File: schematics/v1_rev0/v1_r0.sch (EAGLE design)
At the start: 46 parts, among them Q1 LPM2302, Q2 LPM2302, Q3 16MHz, U1 ATMEGA*, U2 TMP36F

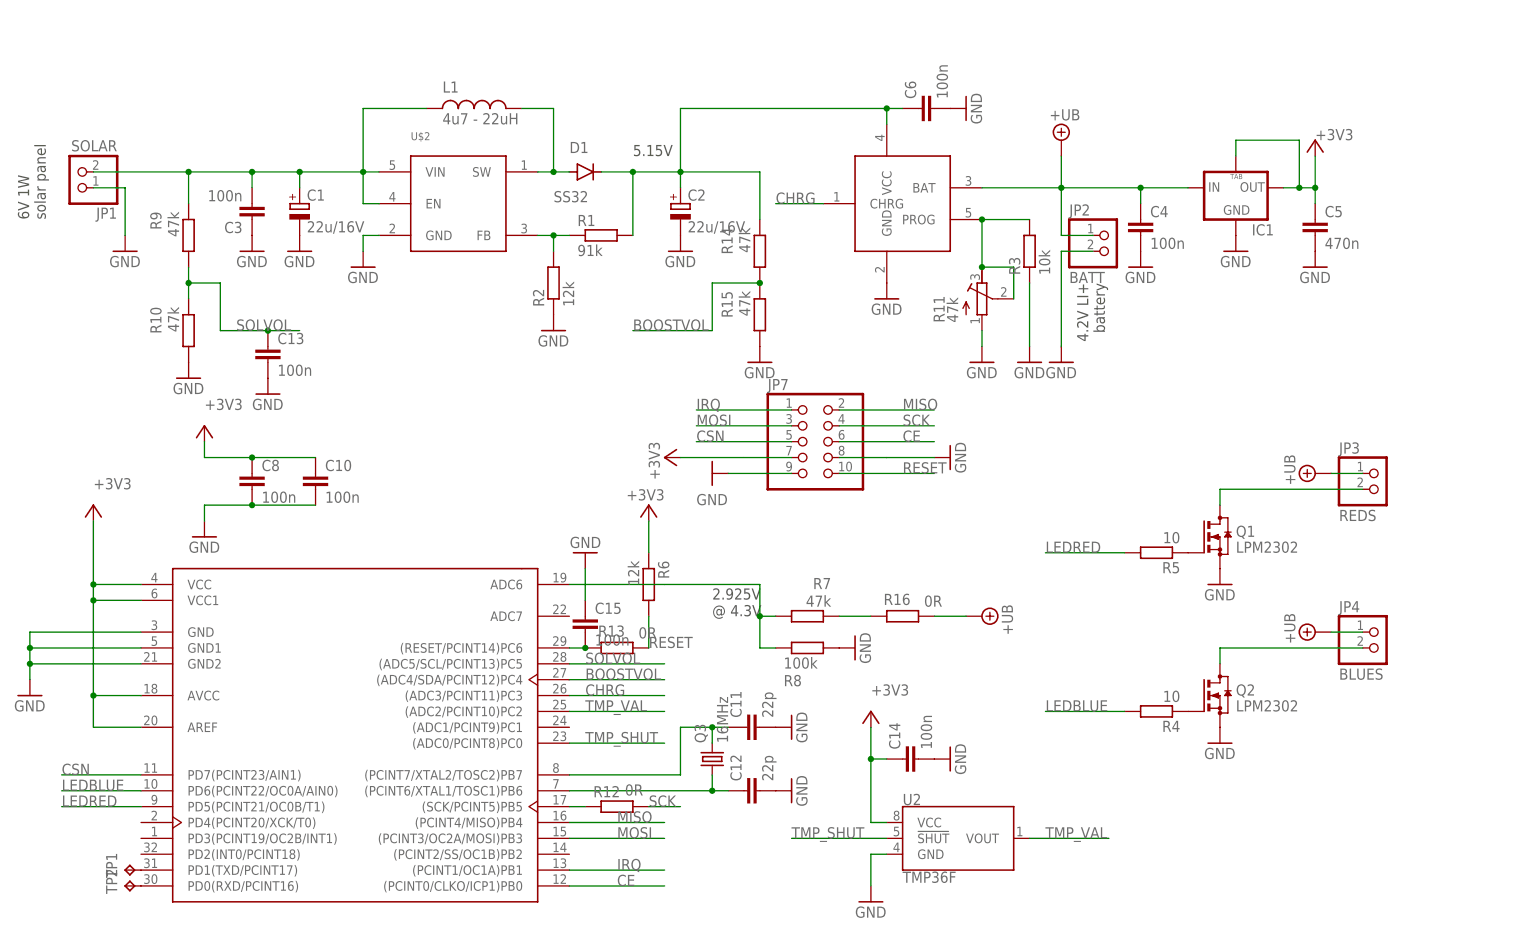
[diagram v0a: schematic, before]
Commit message: even newser schematics
WARNING: replace AMS1117 with MAX8888
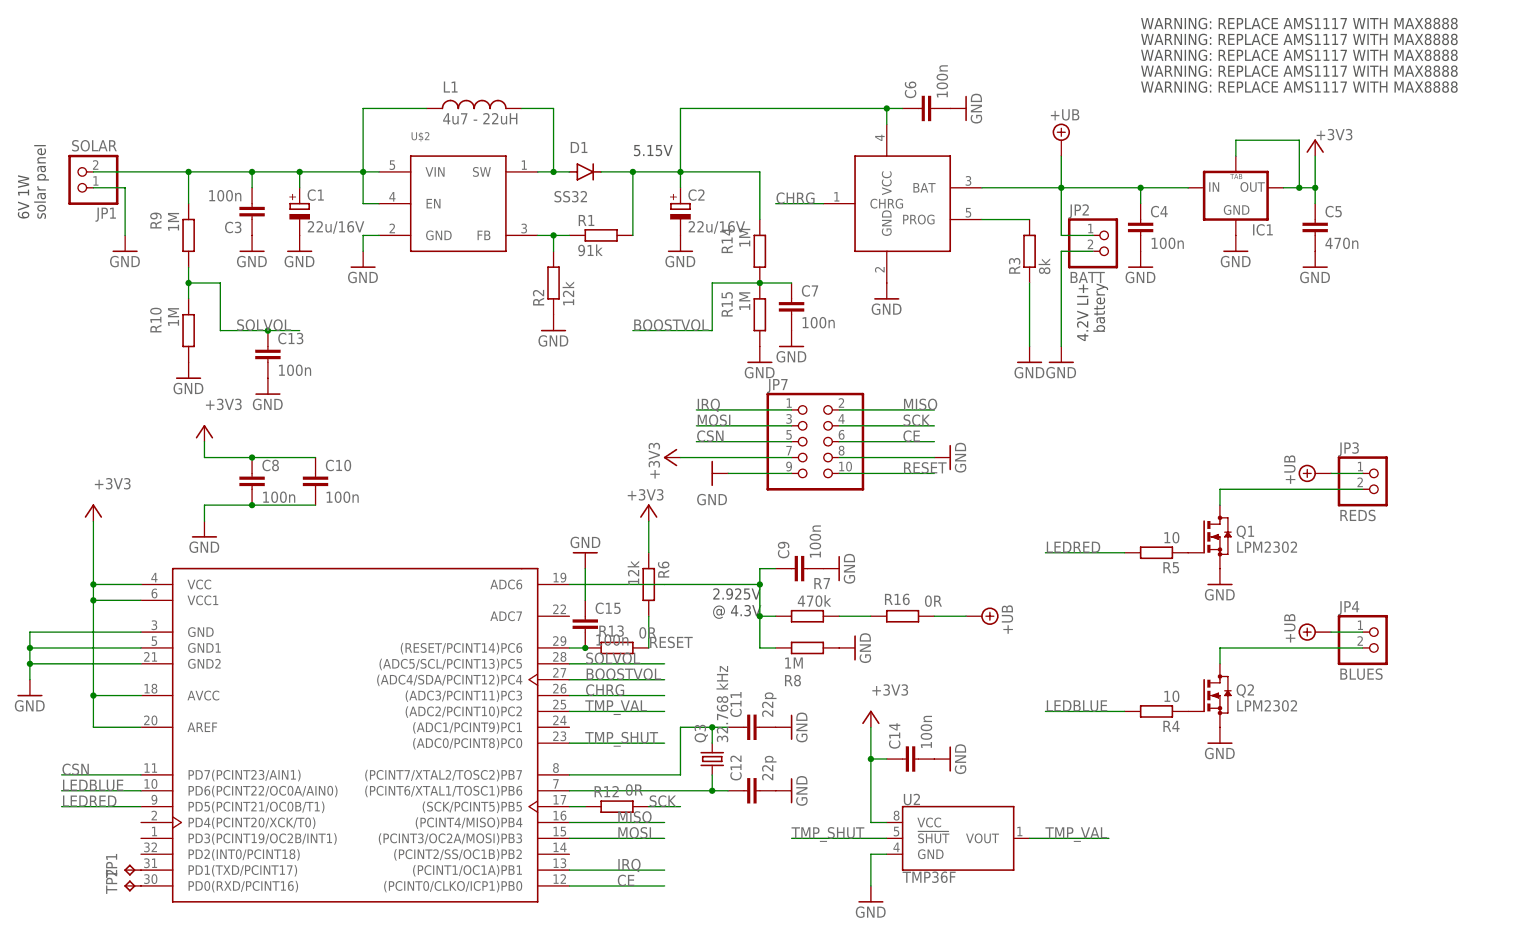
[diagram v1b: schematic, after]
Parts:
- removed R11: 47k, resistor:R-TRIMMCVR42A
- added C7, C9: 100n, rcl:C-EUC0603
- Q3: value 16MHz -> 32.768 kHz
- R10, R14, R15, R9: value 47k -> 1M
- R3: value 10k -> 8k
- R7: value 47k -> 470k
- R8: value 100k -> 1M
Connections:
- net BOOSTVOL: now also C7.1
- net GND: now also C7.2, C9.2; no longer R11.A
- net N$1: no longer R11.E, R11.S
- net N$9: now also C9.1
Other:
- note added: "WARNING: REPLACE AMS1117 WITH MAX8888"
